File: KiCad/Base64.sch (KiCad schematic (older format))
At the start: 21 parts, among them J1 1473149-1, J2 Conn_01x03, U1 501MLFT, U2 SN74CBTD3861DGVR, U3 SN74CBTD3861DGVR, U4 SN74CBTD3861DGVR, U5 SN74CBTD3861DGVR, U6 SN74CBTD3861DGVR, U7 SN74CBTD3861DGVR, U8 SN74CBTD3861DGVR, U9 68000_PinHeader

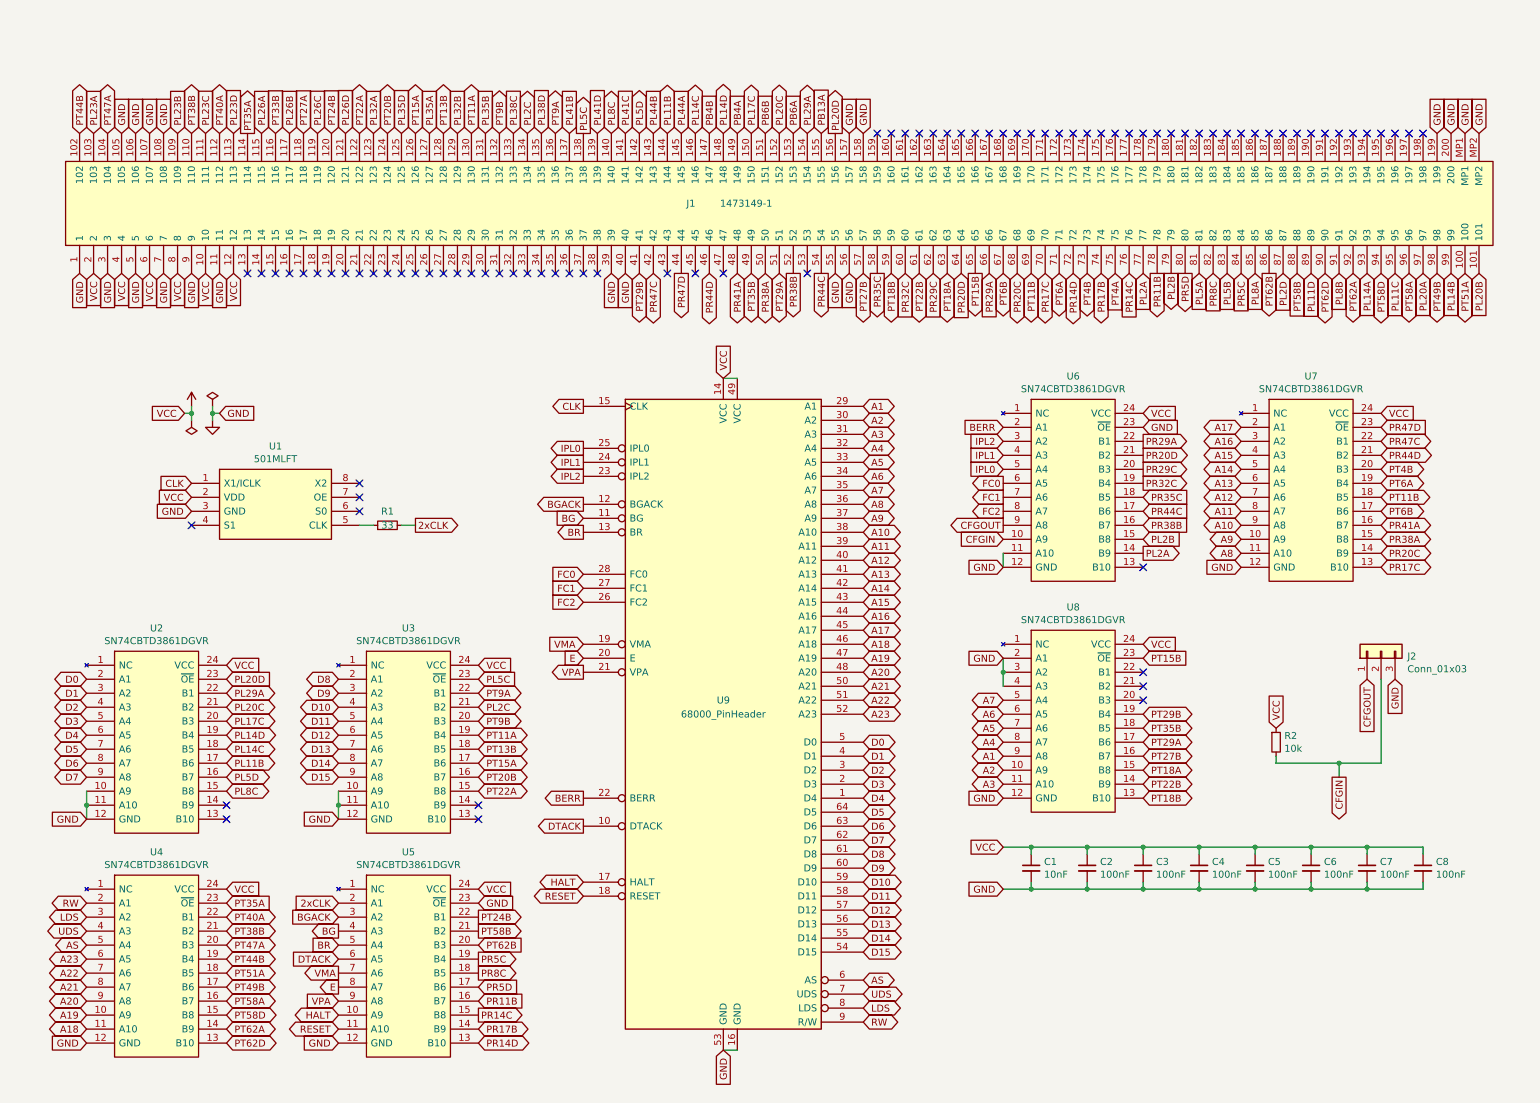
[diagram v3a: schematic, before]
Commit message: Add a 74AHCT1G17 buffering the raw 7 MHz clk and fanout to the 501 PLL (U1) and a pin in the CBTD (U6) that propagates to PL23A (J1 on the FPGA)
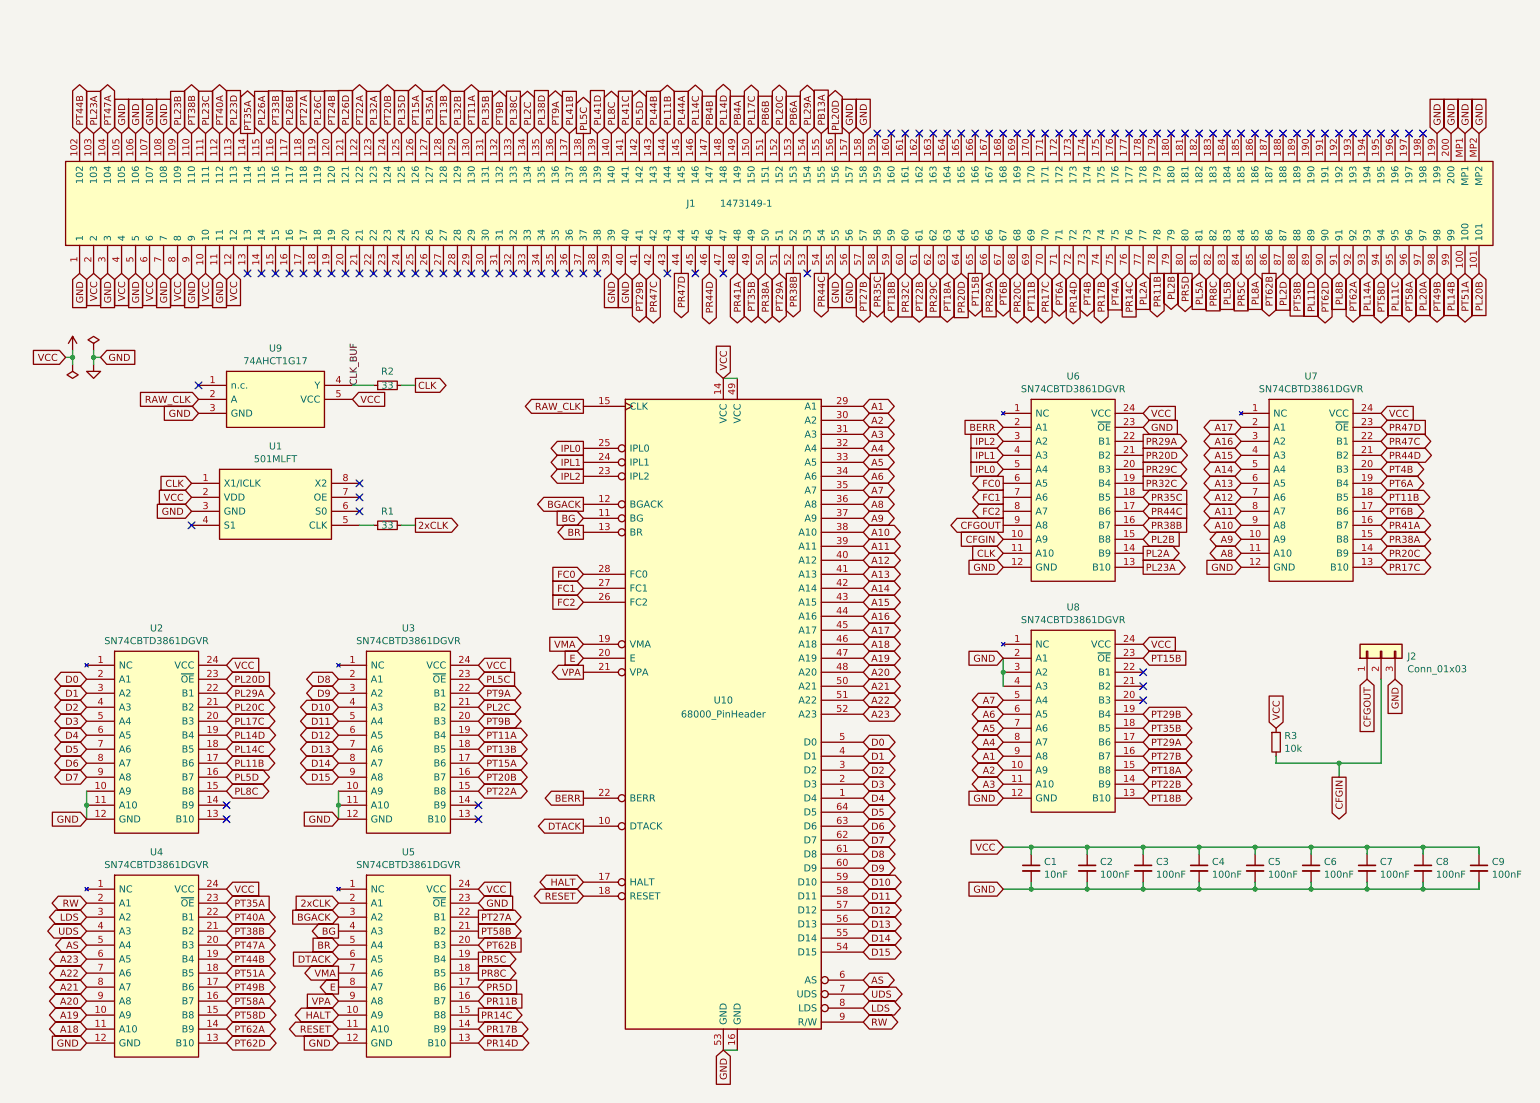
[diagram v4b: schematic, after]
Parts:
- added C9: 100nF, Capacitor_SMD:C_0603_1608Metric, symbol Device:C_Small
- added R2: 33, Resistor_SMD:R_0603_1608Metric, symbol Device:R_Small
- added U9: 74AHCT1G17, Base64:SOT95P275X110-5N, symbol Base64:74AHCT1G17
- renumbered R2 to R3, U9 to U10
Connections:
- net CLK: now also U6.11 (A10), R2.2; no longer U10.15 (CLK)
- net GND: now also C9.2, U9.3 (GND); no longer U6.11 (A10)
- net PL23A: now also U6.13 (B10)
- net PT24B: no longer U5.22 (B1)
- net PT27A: now also U5.22 (B1)
- net VCC: now also C9.1, U9.5 (VCC)
- new net CLK_BUF: R2.1, U9.4 (Y)
- new net RAW_CLK: U10.15 (CLK), U9.2 (A)
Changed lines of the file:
@@
 L power:VCC #PWR0101
 U 1 1 66BFF4F3
-P 1700 2900
-F 0 "#PWR0101" H 1715 3073 50  0001 C CNN
-F 1 "VCC" H 1715 3073 50  0001 C CNN
-F 2 "" H 1700 2900 50  0001 C CNN
-F 3 "" H 1700 2900 50  0001 C CNN
-	1    1700 2900
+P 850 2500
+F 0 "#PWR0101" H 865 2673 50  0001 C CNN
+F 1 "VCC" H 865 2673 50  0001 C CNN
+F 2 "" H 850 2500 50  0001 C CNN
+F 3 "" H 850 2500 50  0001 C CNN
+	1    850  2500
 	1    0    0    -1
 $EndComp
@@
 L power:PWR_FLAG #FLG0101
 U 1 1 66BFFF76
-P 1700 3000
-F 0 "#FLG0101" H 1700 3075 50  0001 C CNN
-F 1 "PWR_FLAG" H 1700 3173 50  0001 C CNN
-F 2 "" H 1700 3000 50  0001 C CNN
-F 3 "~" H 1700 3000 50  0001 C CNN
-	1    1700 3000
+P 850 2600
+F 0 "#FLG0101" H 850 2675 50  0001 C CNN
+F 1 "PWR_FLAG" H 850 2773 50  0001 C CNN
+F 2 "" H 850 2600 50  0001 C CNN
+F 3 "~" H 850 2600 50  0001 C CNN
+	1    850  2600
 	-1   0    0    1
 $EndComp
-Text GLabel 1650 2950 0    50   Input ~ 0
-VCC
-Wire Wire Line
-	1700 2900 1700 2950
-Wire Wire Line
-	1650 2950 1700 2950
-Connection ~ 1700 2950
-Wire Wire Line
-	1700 2950 1700 3000
+Text GLabel 800  2550 0    50   Input ~ 0
+VCC
+Wire Wire Line
+	850  2500 850  2550
+Wire Wire Line
+	800  2550 850  2550
+Connection ~ 850  2550
+Wire Wire Line
+	850  2550 850  2600
 $Comp
 L power:PWR_FLAG #FLG0102
 U 1 1 66C0324F
-P 1850 2900
-F 0 "#FLG0102" H 1850 2975 50  0001 C CNN
-F 1 "PWR_FLAG" H 1850 3073 50  0001 C CNN
-F 2 "" H 1850 2900 50  0001 C CNN
-F 3 "~" H 1850 2900 50  0001 C CNN
-	1    1850 2900
+P 1000 2500
+F 0 "#FLG0102" H 1000 2575 50  0001 C CNN
+F 1 "PWR_FLAG" H 1000 2673 50  0001 C CNN
+F 2 "" H 1000 2500 50  0001 C CNN
+F 3 "~" H 1000 2500 50  0001 C CNN
+	1    1000 2500
 	1    0    0    -1
 $EndComp
@@
 L power:GND #PWR0102
 U 1 1 66C03B19
-P 1850 3000
-F 0 "#PWR0102" H 1850 2750 50  0001 C CNN
-F 1 "GND" H 1855 2827 50  0001 C CNN
-F 2 "" H 1850 3000 50  0001 C CNN
-F 3 "" H 1850 3000 50  0001 C CNN
-	1    1850 3000
-	1    0    0    -1
-$EndComp
-Text GLabel 1900 2950 2    50   Input ~ 0
-GND
-Wire Wire Line
-	1850 2900 1850 2950
-Wire Wire Line
-	1900 2950 1850 2950
-Connection ~ 1850 2950
-Wire Wire Line
-	1850 2950 1850 3000
-$Comp
-L CPU_NXP_68000:68000D U9
+P 1000 2600
+F 0 "#PWR0102" H 1000 2350 50  0001 C CNN
+F 1 "GND" H 1005 2427 50  0001 C CNN
+F 2 "" H 1000 2600 50  0001 C CNN
+F 3 "" H 1000 2600 50  0001 C CNN
+	1    1000 2600
+	1    0    0    -1
+$EndComp
+Text GLabel 1050 2550 2    50   Input ~ 0
+GND
+Wire Wire Line
+	1000 2500 1000 2550
+Wire Wire Line
+	1050 2550 1000 2550
+Connection ~ 1000 2550
+Wire Wire Line
+	1000 2550 1000 2600
+$Comp
+L CPU_NXP_68000:68000D U10
 U 1 1 68E7DFB3
 P 5500 5100
-F 0 "U9" H 5500 5200 50  0000 C CNN
+F 0 "U10" H 5500 5200 50  0000 C CNN
 F 1 "68000_PinHeader" H 5500 5100 50  0000 C CNN
 F 2 "Package_DIP:DIP-64_W22.86mm" H 5500 5100 50  0001 C CNN
@@
 IPL2
 Text GLabel 4500 2900 0    50   Output ~ 0
-CLK
+RAW_CLK
 Text GLabel 4500 5700 0    50   Output ~ 0
 BERR
@@
 NoConn ~ 2900 3450
 NoConn ~ 1700 3750
-Text GLabel 1700 3450 0    50   Input ~ 0
-CLK
+Text GLabel 1750 2850 0    50   Input ~ 0
+RAW_CLK
 NoConn ~ 2900 3550
 NoConn ~ 2900 3650
@@
 Text GLabel 3750 5350 2    50   BiDi ~ 0
 PT13B
-Text GLabel 3750 6550 2    50   Output ~ 0
-PT24B
 Text GLabel 950  7450 0    50   Input ~ 0
 GND
@@
 Text GLabel 3750 4750 2    50   Input ~ 0
 VCC
-NoConn ~ 3750 5750
 NoConn ~ 3750 5850
 $Comp
@@
 Text GLabel 7500 3750 0    50   Output ~ 0
 CFGOUT
-Wire Wire Line
-	7500 3950 7500 4050
-NoConn ~ 8500 4050
 $Comp
 L Device:R_Small R1
@@
 Connection ~ 10100 6350
 $Comp
-L Device:R_Small R2
+L Device:R_Small R3
 U 1 1 691CD8B3
 P 9450 5300
-F 0 "R2" H 9509 5346 50  0000 L CNN
+F 0 "R3" H 9509 5346 50  0000 L CNN
 F 1 "10k" H 9509 5255 50  0000 L CNN
 F 2 "Resistor_SMD:R_0603_1608Metric" H 9450 5300 50  0001 C CNN
@@
 	2750 5750 2750 5850
 Wire Wire Line
+	950  5650 950  5750
+Connection ~ 950  5750
+Wire Wire Line
+	9450 5400 9450 5450
+Wire Wire Line
+	9450 5450 9900 5450
+Wire Wire Line
+	9900 5450 10200 5450
+Wire Wire Line
+	10200 5450 10200 4850
+Connection ~ 9900 5450
+Wire Wire Line
+	9900 5450 9900 5550
+Text GLabel 6500 950  1    50   Input ~ 0
+GND
+$Comp
+L Base64:74AHCT1G17 U9
+U 1 1 6906FEE7
+P 2300 2850
+F 0 "U9" H 2300 3215 50  0000 C CNN
+F 1 "74AHCT1G17" H 2300 3124 50  0000 C CNN
+F 2 "Base64:SOT95P275X110-5N" H 2700 3050 50  0001 L CNN
+F 3 "" H 2700 2950 50  0001 L CNN
+	1    2300 2850
+	1    0    0    -1
+$EndComp
+NoConn ~ 1750 2750
+Text GLabel 1700 3450 0    50   Input ~ 0
+CLK
+Text GLabel 2850 2850 2    50   Input ~ 0
+VCC
+Text GLabel 1750 2950 0    50   Input ~ 0
+GND
+Text GLabel 3750 6550 2    50   Output ~ 0
+PT27A
+Text GLabel 3300 2750 2    50   Output ~ 0
+CLK
+Text GLabel 7500 3950 0    50   Input ~ 0
+CLK
+$Comp
+L Device:R_Small R2
+U 1 1 690B0985
+P 3100 2750
+F 0 "R2" V 3200 2750 50  0000 C CNN
+F 1 "33" V 3100 2750 50  0000 C CNN
+F 2 "Resistor_SMD:R_0603_1608Metric" H 3100 2750 50  0001 C CNN
+F 3 "~" H 3100 2750 50  0001 C CNN
+	1    3100 2750
+	0    -1   -1   0
+$EndComp
+Wire Wire Line
+	3200 2750 3300 2750
+Wire Wire Line
+	3000 2750 2850 2750
+Text Label 2900 2750 1    50   ~ 0
+CLK_BUF
+Wire Wire Line
 	2750 5650 2750 5750
 Connection ~ 2750 5750
-Wire Wire Line
-	950  5650 950  5750
-Connection ~ 950  5750
-Wire Wire Line
-	9450 5400 9450 5450
-Wire Wire Line
-	9450 5450 9900 5450
-Wire Wire Line
-	9900 5450 10200 5450
-Wire Wire Line
-	10200 5450 10200 4850
-Connection ~ 9900 5450
-Wire Wire Line
-	9900 5450 9900 5550
-Text GLabel 6500 950  1    50   Input ~ 0
-GND
+NoConn ~ 3750 5750
+Text GLabel 8500 4050 2    50   Output ~ 0
+PL23A
+$Comp
+L Device:C_Small C9
+U 1 1 6912AA71
+P 10900 6200
+F 0 "C9" H 10992 6246 50  0000 L CNN
+F 1 "100nF" H 10992 6155 50  0000 L CNN
+F 2 "Capacitor_SMD:C_0603_1608Metric" H 10900 6200 50  0001 C CNN
+F 3 "~" H 10900 6200 50  0001 C CNN
+	1    10900 6200
+	1    0    0    -1
+$EndComp
+Wire Wire Line
+	10900 6100 10900 6050
+Wire Wire Line
+	10900 6050 10500 6050
+Connection ~ 10500 6050
+Wire Wire Line
+	10900 6300 10900 6350
+Wire Wire Line
+	10900 6350 10500 6350
+Connection ~ 10500 6350
 $EndSCHEMATC

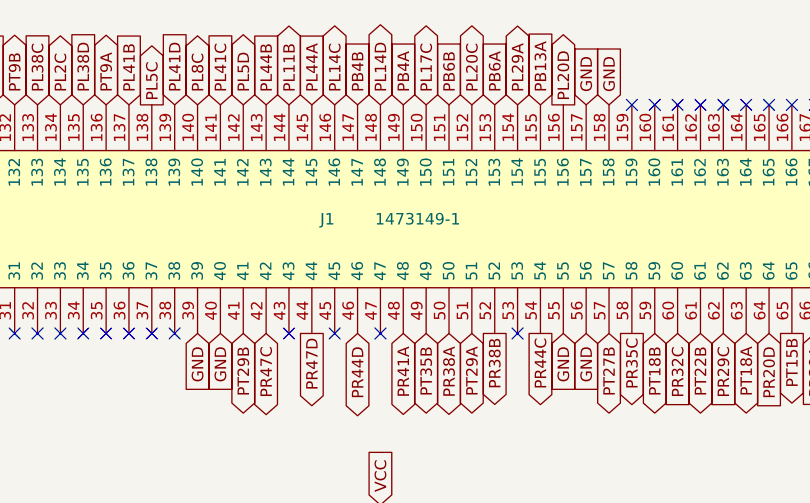
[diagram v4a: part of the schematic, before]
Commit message: Change J1 value from 1473149-1 (SO-DIMM DDR) to 1473149-4 (SO-DIMM DDR2) as keying is different and iCESugar-Pro module is of DDR2 type.
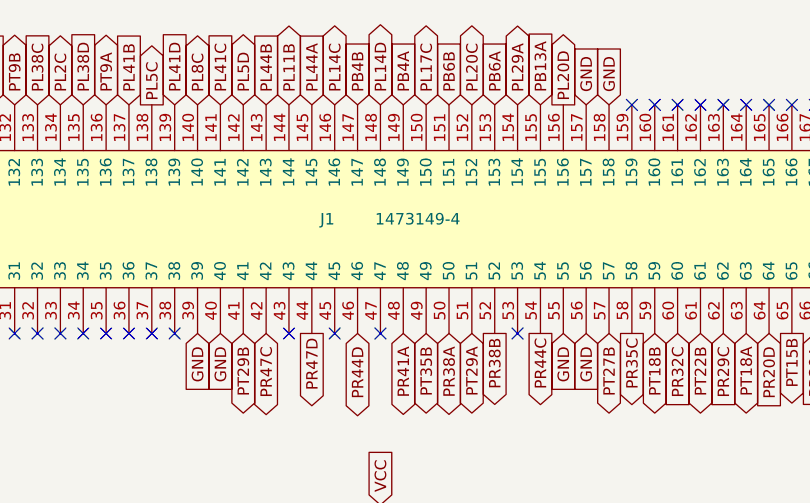
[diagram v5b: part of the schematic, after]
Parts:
- J1: value 1473149-1 -> 1473149-4
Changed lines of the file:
@@
 P 900 1950
 F 0 "J1" V 1400 -2450 50  0000 L CNN
-F 1 "1473149-1" V 1400 -3000 50  0000 L CNN
+F 1 "1473149-4" V 1400 -3000 50  0000 L CNN
 F 2 "Base64:TE_DDR2-SODIMM-200_1473149-x" H 1750 2050 50  0001 L CNN
 F 3 "https://www.te.com/commerce/DocumentDelivery/DDEController?Action=srchrtrv&DocNm=1473149&DocType=Customer+Drawing&DocLang=English" H 1750 1950 50  0001 L CNN
